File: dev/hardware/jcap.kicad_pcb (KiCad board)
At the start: 2 copper layers, 115.6 x 87 mm, 52 parts, among them J201 CPU PGMR, J202 GPU PGMR, J203 SPARE GPU HDR, J204 SPARE CPU HDR, J301 DC IN, J502 VGA OUT, J601 CONTROLS, SW201 CPU ~{RES}, SW202 GPU ~{RES}, SW203 DEBUG, SW601 TILT, U101 P8X32A-D40, U201 P8X32A-D40, U302 LF33_TO220, U401 24LC256, U402 24LC256, U601 74HC165, U602 74HC165, Y101 6.5MHz, Y201 6.5MHz

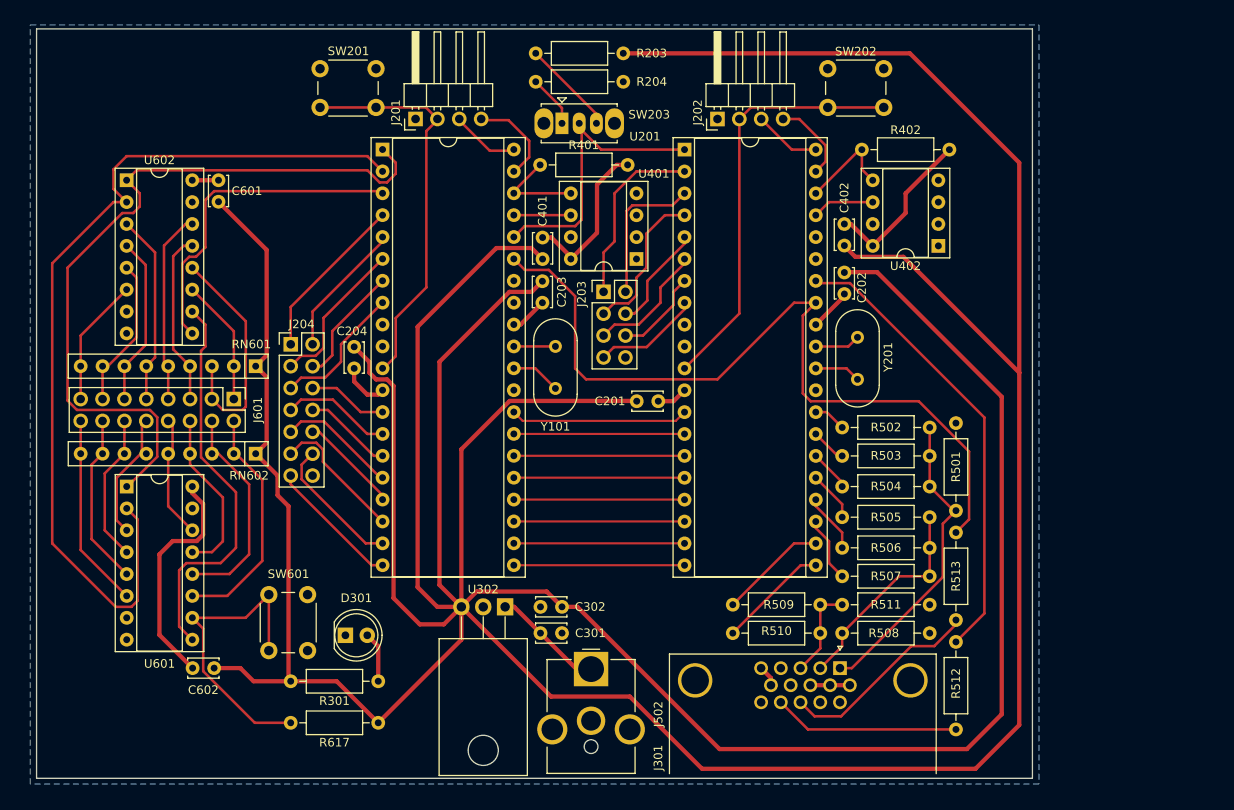
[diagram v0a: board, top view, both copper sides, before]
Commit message: Added silkscreen - review ready
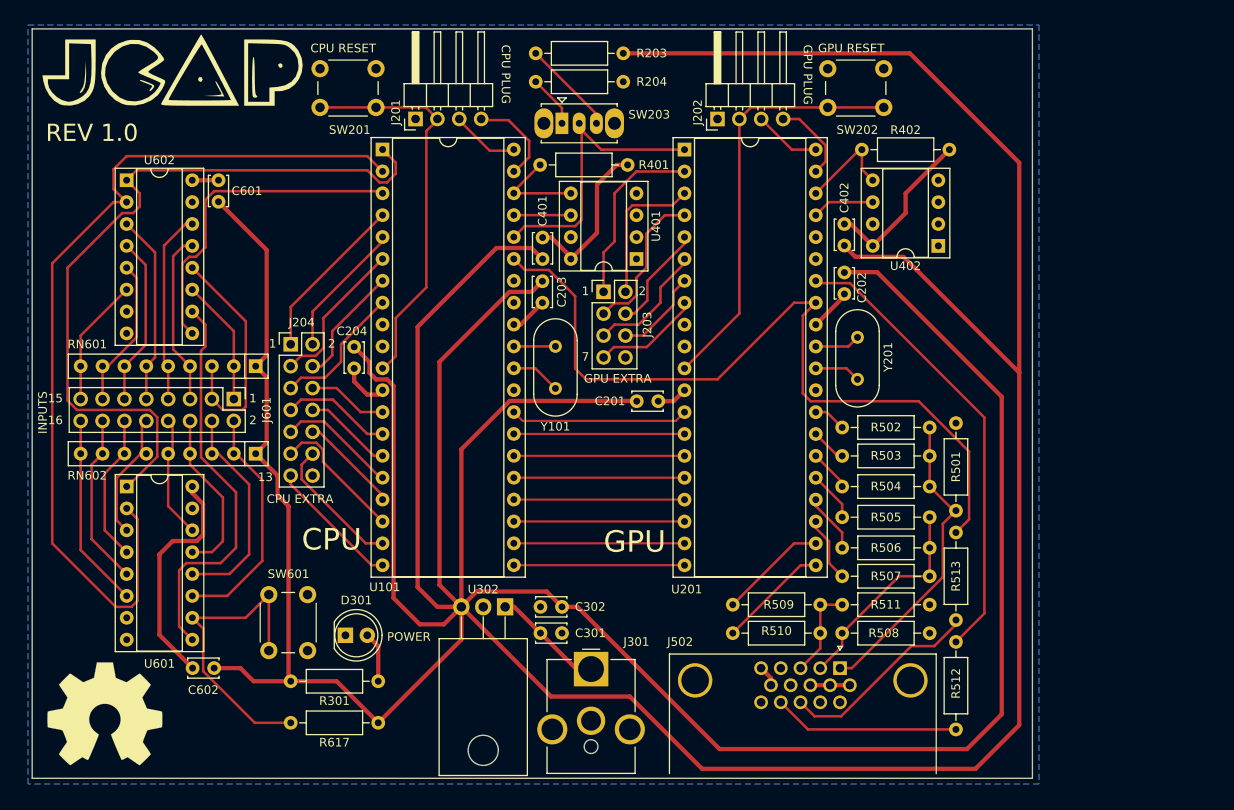
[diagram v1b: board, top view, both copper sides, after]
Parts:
- added G***: LOGO, LOGO, F.Cu at (114.6, 70.6)
- added REF**: OSHW-Symbol_13.4x12mm_SilkScreen, Symbol:OSHW-Symbol_13.4x12mm_SilkScreen, F.Cu at (106.7, 145.5)
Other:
- board size 115.6 x 87 mm -> 116.1 x 87 mm
- board text added: "1"
- board text added: "13"
- board text added: "15"
- board text added: "16"
- board text added: "2"
- board text added: "7"
- board text added: "CPU"
- board text added: "CPU EXTRA"
- board text added: "CPU PLUG"
- board text added: "CPU RESET"
- board text added: "GPU"
- board text added: "GPU EXTRA"
- board text added: "GPU PLUG"
- board text added: "GPU RESET"
- board text added: "INPUTS"
- board text added: "POWER"
- board text added: "REV 1.0"

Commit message: Finalized review schematic & pcb
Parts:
- moved C202 2.55 mm to (192.5, 94.2), turned to -90 degrees
- moved C201 2.54 mm to (168.4, 109.2), turned to 0 degrees
- moved C601 2.54 mm to (119.9, 86.1), turned to 90 degrees
- moved C203 2.52 mm to (157.5, 95.3), turned to -90 degrees
- moved C204 2.52 mm to (135.6, 102.9), turned to -90 degrees
- moved C602 2.50 mm to (119.4, 140.2), turned to 180 degrees
- moved G*** 0.25 mm to (114.3, 70.6)
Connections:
- C201 pad 1: Net-(C201-Pad1) -> GND
- C202 pad 1: Net-(C202-Pad1) -> GND
- C203 pad 1: Net-(C203-Pad1) -> GND
- C204 pad 1: Net-(C204-Pad1) -> GND
- C401 pad 1: Net-(U401-VCC) -> GND
- C402 pad 1: Net-(U402-VCC) -> GND
- C601 pad 1: Net-(U602-VCC) -> GND
- C602 pad 1: Net-(U601-VCC) -> GND
- R401 pad 2: Net-(U401-VCC) -> +3.3V
- R402 pad 2: Net-(U402-VCC) -> +3.3V
- U101 pad 12: Net-(C204-Pad1) -> +3.3V
- U101 pad 32: Net-(C203-Pad1) -> +3.3V
- U201 pad 12: Net-(C201-Pad1) -> +3.3V
- U201 pad 32: Net-(C202-Pad1) -> +3.3V
- U401 pad 8: Net-(U401-VCC) -> +3.3V
- U402 pad 8: Net-(U402-VCC) -> +3.3V
- U601 pad 16: Net-(U601-VCC) -> +3.3V
- U602 pad 16: Net-(U602-VCC) -> +3.3V
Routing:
- net Net-(U601-VCC): track 26.9 -> 0.00 mm
- net +3.3V: track 635.1 -> 614.7 mm
- net Net-(U402-VCC): track 19.5 -> 0.00 mm
- net Net-(U401-VCC): track 18.9 -> 0.00 mm
- net Net-(U601-DS): track 35.9 -> 25.9 mm
- net INPUTS: track 38.6 -> 47.5 mm
- net H_SYNC: track 53.6 -> 60.1 mm
- net Net-(C204-Pad1): track 5.68 -> 0.00 mm
- net Net-(C202-Pad1): track 5.45 -> 0.00 mm
- net Net-(C203-Pad1): track 4.36 -> 0.00 mm
- net Net-(C201-Pad1): track 3.58 -> 0.00 mm
- net Net-(U602-VCC): track 3.05 -> 0.00 mm
- net ~{INPUTS_PL}: track 87.4 -> 88.5 mm
- net INPUTS_CLK: track 105.6 -> 106.5 mm
- net V_SYNC: track 92.7 -> 92.1 mm
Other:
- board size 116.1 x 87 mm -> 115 x 87 mm

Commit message: Thicc-traced VGA sig test - REVERT HERE
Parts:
- removed REF**: OSHW-Symbol_13.4x12mm_SilkScreen, Symbol:OSHW-Symbol_13.4x12mm_SilkScreen
- added R502: 309, Resistor_THT:R_Axial_DIN0207_L6.3mm_D2.5mm_P10.16mm_Horizontal, F.Cu at (212.6, 126.2)
- added R503: 309, Resistor_THT:R_Axial_DIN0207_L6.3mm_D2.5mm_P10.16mm_Horizontal, F.Cu at (209.3, 126.2)
- added R505: 154, Resistor_THT:R_Axial_DIN0207_L6.3mm_D2.5mm_P10.16mm_Horizontal, F.Cu at (205.5, 128.8)
- added R517: 266, Resistor_THT:R_Axial_DIN0207_L6.3mm_D2.5mm_P10.16mm_Horizontal, F.Cu at (187.2, 132.7)
- added R518: 266, Resistor_THT:R_Axial_DIN0207_L6.3mm_D2.5mm_P10.16mm_Horizontal, F.Cu at (187.2, 136.1)
- added R519: 133, Resistor_THT:R_Axial_DIN0207_L6.3mm_D2.5mm_P10.16mm_Horizontal, F.Cu at (189.7, 132.6)
- added R520: 266, Resistor_THT:R_Axial_DIN0207_L6.3mm_D2.5mm_P10.16mm_Horizontal, F.Cu at (189.7, 136.0)
- added R521: 173, Resistor_THT:R_Axial_DIN0207_L6.3mm_D2.5mm_P10.16mm_Horizontal, F.Cu at (202.4, 129.3)
- R501: value 150 -> 309
- R504: renamed from R502; value 270 -> 154
- R506: renamed from R503; value 560 -> 309
- R507: renamed from R504; value 1.1K -> 146
- R508: renamed from R505; value 270 -> 309
- R509: renamed from R506; value 560 -> 309
- R510: renamed from R507; value 1.1K -> 309
- R511: renamed from R508; value 150 -> 154
- R512: renamed from R509; value 270 -> 154
- R513: renamed from R510; value 470 -> 309
- R516: renamed from R511; value 150 -> 146
- moved R507 30.6 mm to (223.0, 141.7)
- moved R504 28.3 mm to (222.0, 132.7)
- moved R514 27.2 mm to (223.0, 145.3), turned to 180 degrees
- moved R513 25.8 mm to (206.0, 116.1), turned to -90 degrees
- moved R506 24.3 mm to (208.8, 139.0), turned to 90 degrees
- moved R516 19.8 mm to (222.0, 136.1)
- moved R501 17.8 mm to (215.9, 126.2), turned to 90 degrees
- moved R512 14.5 mm to (202.7, 126.2), turned to 90 degrees
- moved R511 11.6 mm to (211.8, 129.3), turned to 0 degrees
- moved R508 10.3 mm to (192.8, 126.2), turned to 90 degrees
- moved R515 7.51 mm to (212.9, 148.8), turned to 0 degrees
- moved R509 6.37 mm to (196.1, 126.2), turned to 90 degrees
- moved R510 4.51 mm to (199.4, 126.2), turned to 90 degrees
- renumbered C203 to C201, C204 to C202, C201 to C203, C202 to C204, J204 to J202, J202 to J203, J203 to J204, J502 to J501, R203 to R201, R204 to R202, R513 to R514, R512 to R515, R617 to R601, SW203 to SW202, SW202 to SW203, U101 to U201, U201 to U202, U302 to U301, U602 to U601, U601 to U602, Y101 to Y201, Y201 to Y202
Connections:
- R501 pad 1: GND -> /VGA_DAC/RED_OUT
- R501 pad 2: /VGA_DAC/RED_OUT -> RED1
- R504 pad 2: RED1 -> Net-(R502-Pad1)
- R506 pad 1: /VGA_DAC/RED_OUT -> Net-(R503-Pad1)
- R506 pad 2: RED2 -> GND
- R507 pad 1: /VGA_DAC/RED_OUT -> GND
- R507 pad 2: RED3 -> /VGA_DAC/RED_OUT
- R509 pad 1: /VGA_DAC/GREEN_OUT -> Net-(R509-Pad1)
- R510 pad 1: /VGA_DAC/GREEN_OUT -> Net-(R510-Pad1)
- R511 pad 1: GND -> /VGA_DAC/GREEN_OUT
- R511 pad 2: /VGA_DAC/GREEN_OUT -> Net-(R509-Pad1)
- R512 pad 1: /VGA_DAC/BLUE_OUT -> Net-(R509-Pad1)
- R512 pad 2: BLUE1 -> Net-(R510-Pad1)
- R513 pad 1: /VGA_DAC/BLUE_OUT -> Net-(R510-Pad1)
- R513 pad 2: BLUE2 -> GND
- R516 pad 2: /VGA_DAC/BLUE_OUT -> /VGA_DAC/GREEN_OUT
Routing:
- net V_SYNC: track 92.1 -> 128.2 mm
- net Net-(R509-Pad1): track 0.00 -> 33.2 mm
- net /VGA_DAC/GREEN_OUT: track 25.6 -> 58.4 mm
- net H_SYNC: track 60.1 -> 86.6 mm
- net RED1: track 3.80 -> 29.0 mm
- net +3.3V: track 614.7 -> 637.6 mm
- net Net-(R502-Pad1): track 0.00 -> 20.6 mm
- net RED2: track 4.12 -> 24.6 mm
- net /VGA_DAC/RED_OUT: track 35.7 -> 54.2 mm
- net Net-(R503-Pad1): track 0.00 -> 17.6 mm
- net RED3: track 4.83 -> 20.9 mm
- net Net-(R510-Pad1): track 0.00 -> 14.8 mm
- net Net-(R518-Pad1): track 0.00 -> 14.2 mm
- net Net-(J501-Pad14): track 21.9 -> 30.2 mm
- net /VGA_DAC/BLUE_OUT: track 10.9 -> 17.7 mm
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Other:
- board size 115 x 87 mm -> 133 x 87 mm

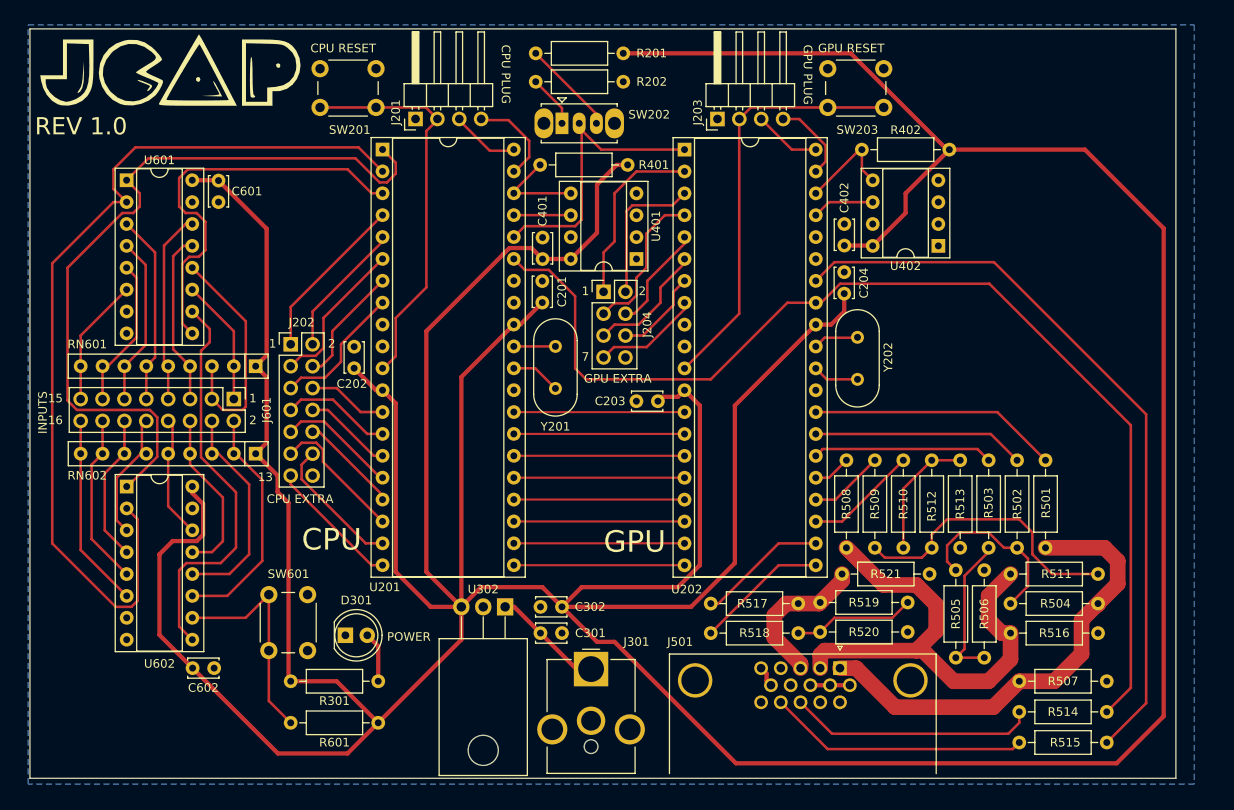
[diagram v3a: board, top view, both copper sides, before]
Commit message: 75 ohm DAC traces final refactor
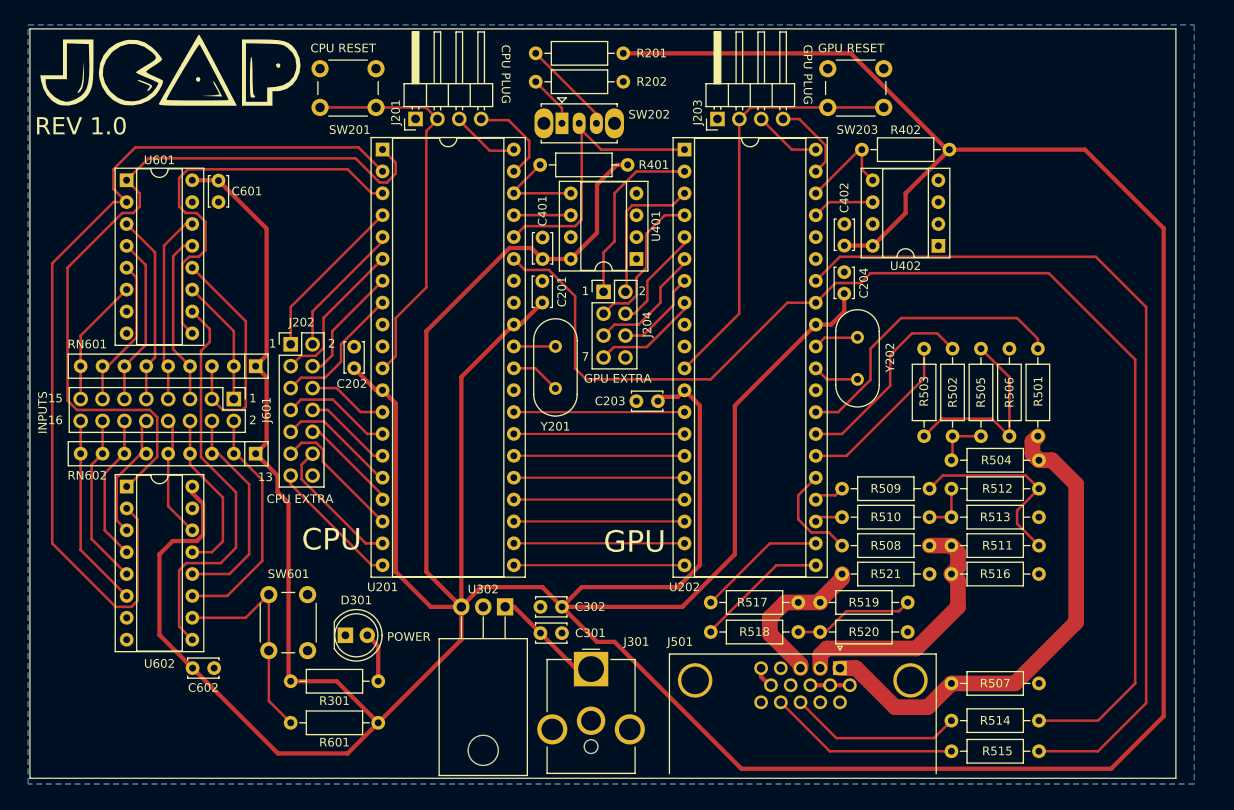
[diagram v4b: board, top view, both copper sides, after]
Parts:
- moved R506 25.9 mm to (211.7, 113.3)
- moved R504 18.0 mm to (215.1, 116.1)
- moved R505 15.8 mm to (208.4, 113.3), turned to 90 degrees
- moved R502 15.0 mm to (205.1, 113.3)
- moved R503 15.0 mm to (201.8, 113.3)
- moved R512 14.2 mm to (215.1, 119.4), turned to 180 degrees
- moved R501 13.0 mm to (215.0, 113.3)
- moved R516 9.70 mm to (215.1, 129.3)
- moved R508 9.66 mm to (202.4, 126.0), turned to 180 degrees
- moved R509 9.35 mm to (202.4, 119.4), turned to 180 degrees
- moved R515 7.94 mm to (205.0, 149.9)
- moved R514 7.94 mm to (215.1, 146.3)
- moved R507 7.88 mm to (215.1, 142.0)
- moved R511 7.61 mm to (205.0, 126.0)
- moved R513 6.68 mm to (205.0, 122.7), turned to 0 degrees
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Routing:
- net /VGA_DAC/GREEN_OUT: track 58.4 -> 30.4 mm
- net H_SYNC: track 86.6 -> 102.7 mm
- net V_SYNC: track 128.2 -> 142.7 mm
- net Net-(R502-Pad1): track 20.6 -> 6.15 mm
- net Net-(R509-Pad1): track 33.2 -> 22.7 mm
- net GREEN3: track 13.1 -> 3.26 mm
- net Net-(R510-Pad1): track 14.8 -> 5.97 mm
- net Net-(J501-Pad13): track 28.7 -> 20.1 mm
- net Net-(J501-Pad14): track 30.2 -> 22.2 mm
- net GREEN1: track 4.40 -> 12.0 mm
- net RED1: track 29.0 -> 34.6 mm
- net Net-(R503-Pad1): track 17.6 -> 23.1 mm
- net GREEN2: track 8.75 -> 3.57 mm
- net /VGA_DAC/RED_OUT: track 54.2 -> 58.2 mm
- net RED3: track 20.9 -> 19.7 mm
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
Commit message: Finalized review PCB #2
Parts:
- added REF**: KiCad-Logo2_6mm_SilkScreen, Symbol:KiCad-Logo2_6mm_SilkScreen, F.Cu at (217.7, 73.9)
- added REF**: OSHW-Logo_11.4x12mm_SilkScreen, Symbol:OSHW-Logo_11.4x12mm_SilkScreen, F.Cu at (217.4, 87.9)
- moved C602 20.1 mm to (117.6, 120.2), turned to -90 degrees
- moved U602 2.53 mm to (106.9, 120.2)
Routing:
- net +3.3V: track 637.5 -> 642.8 mm
- net /Input/IN13: track 15.4 -> 19.6 mm
- net /Input/IN14: track 17.2 -> 20.8 mm
- net /Input/IN15: track 20.0 -> 22.9 mm
- net ~{INPUTS_PL}: track 88.5 -> 91.4 mm
- net Net-(U602-DS): track 25.9 -> 28.7 mm
- net /Input/IN9: track 27.6 -> 30.3 mm
- net /Input/IN10: track 25.3 -> 28.0 mm
- net /Input/IN16: track 22.5 -> 25.2 mm
- net /Input/IN11: track 19.6 -> 22.1 mm
- net /Input/SHIFT_IN: track 46.7 -> 49.0 mm
- net /Input/IN12: track 14.3 -> 15.9 mm
- net INPUTS_CLK: track 106.5 -> 107.6 mm
